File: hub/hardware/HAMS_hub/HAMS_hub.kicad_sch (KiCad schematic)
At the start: 29 parts, among them J1 Conn_01x14, J2 Conn_01x04, J3 Conn_01x04, J4 Conn_01x07, J5 Conn_01x02, J6 Conn_01x04, J7 Conn_01x04, J8 Conn_01x04, J9 Conn_01x04, Q1 NMOS, SW1 SW_Push, U1 TCA9406DC, U2 NCP5501, U3 NRF24L01_Breakout

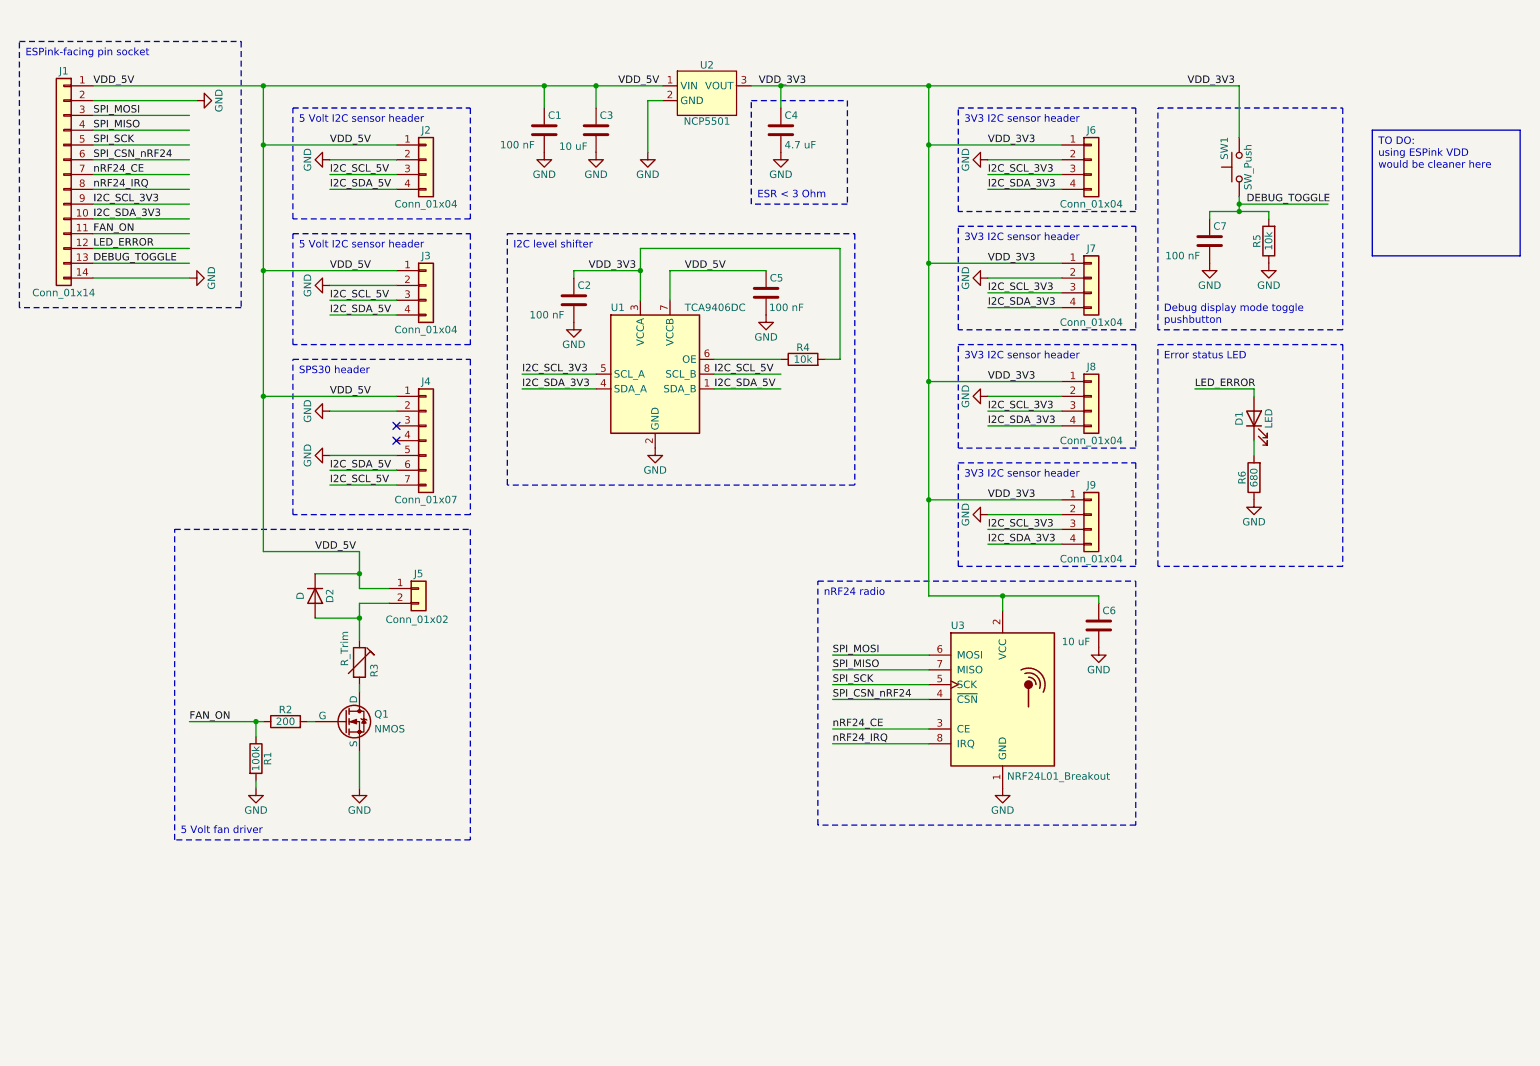
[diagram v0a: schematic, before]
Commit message: Improve HAMS hub HW: schematic and PCB
Improve schematic (add debug headers and mounting holes).
Add DRC-clean PCB design.
Update task list.
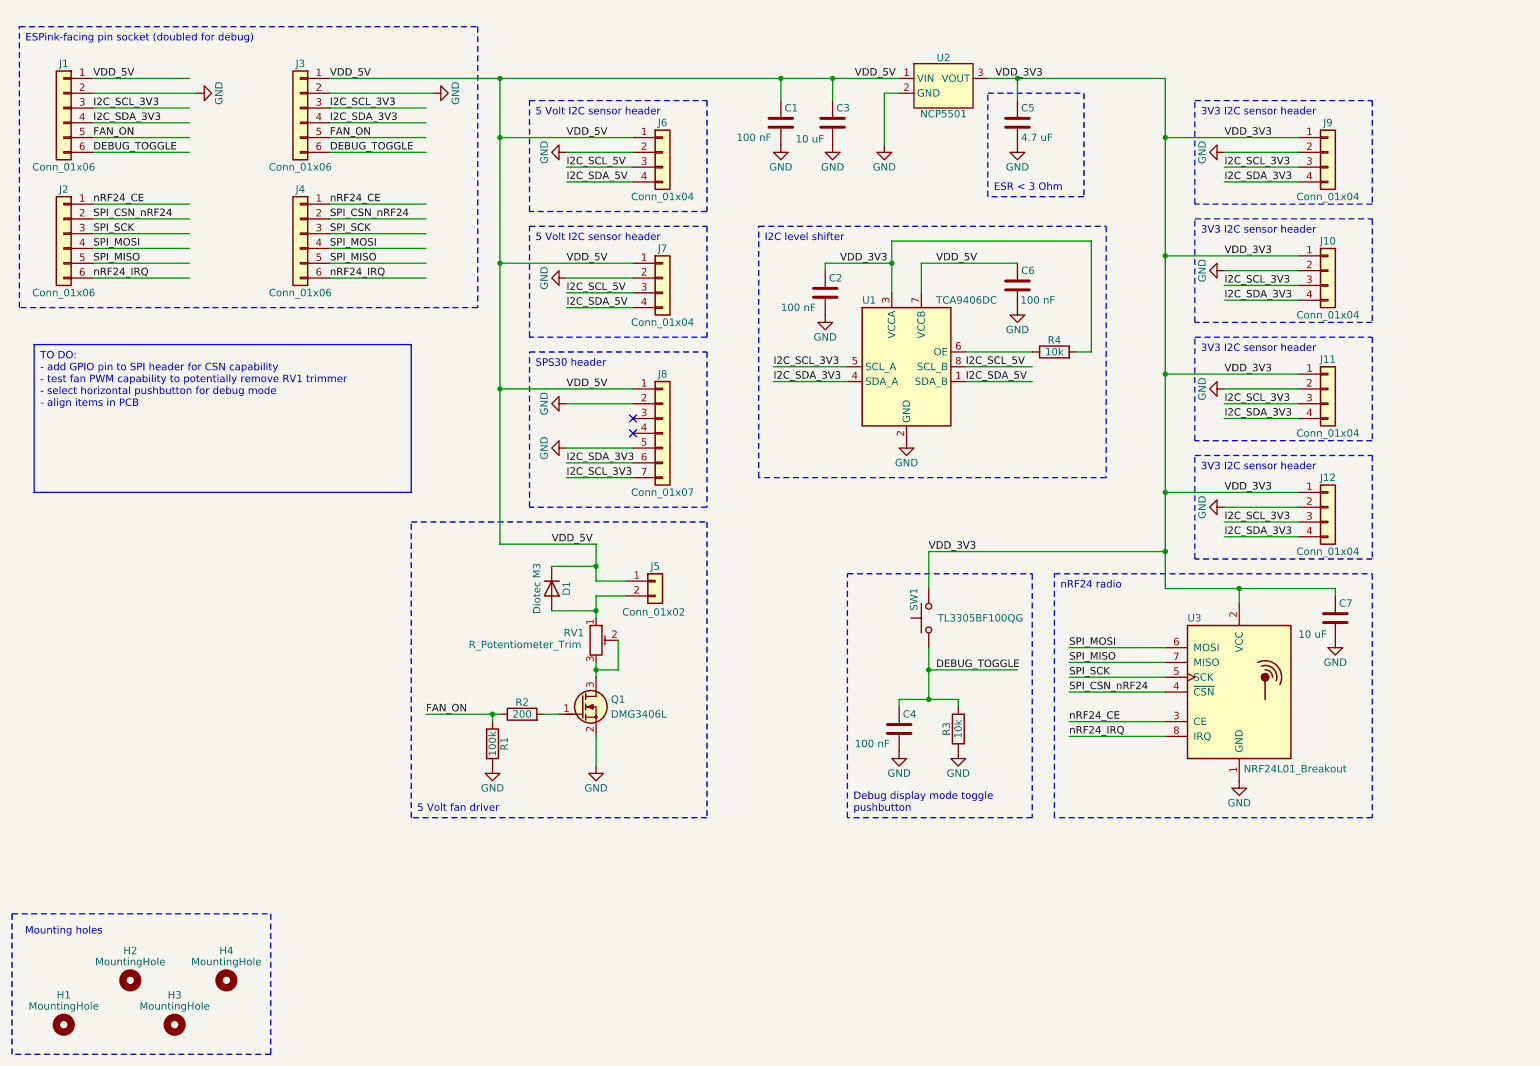
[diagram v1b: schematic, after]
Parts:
- removed D1: LED, symbol Device:LED
- removed J1: Conn_01x14, symbol Connector_Generic:Conn_01x14
- removed Q1: NMOS, symbol Simulation_SPICE:NMOS
- removed R3: R_Trim, symbol Device:R_Trim
- removed R6: 680, symbol Device:R
- added H1, H2, H3, H4: MountingHole, MountingHole:MountingHole_2.5mm, symbol Mechanical:MountingHole
- added J1, J2, J3, J4: Conn_01x06, Connector_PinSocket_2.54mm:PinSocket_1x06_P2.54mm_Vertical, symbol Connector_Generic:Conn_01x06
- added Q1: DMG3406L, PCM_Package_TO_SOT_SMD_AKL:SOT-23, symbol PCM_Transistor_MOSFET_AKL:DMG3406L
- added RV1: R_Potentiometer_Trim, PCM_Potentiometer_SMD_AKL:Potentiometer_Bourns_3269W_Vertical, symbol Device:R_Potentiometer_Trim
- C1, C2, C3: footprint (none) -> Capacitor_SMD:C_0805_2012Metric_Pad1.18x1.45mm_HandSolder
- C4: renamed from C7; footprint (none) -> Capacitor_SMD:C_0805_2012Metric_Pad1.18x1.45mm_HandSolder
- C5: renamed from C4; footprint (none) -> Capacitor_SMD:C_0805_2012Metric_Pad1.18x1.45mm_HandSolder
- C6: renamed from C5; footprint (none) -> Capacitor_SMD:C_0805_2012Metric_Pad1.18x1.45mm_HandSolder
- C7: renamed from C6; footprint (none) -> Capacitor_SMD:C_0805_2012Metric_Pad1.18x1.45mm_HandSolder
- D1: renamed from D2; value D -> Diotec M3; footprint (none) -> Diode_SMD:D_SMA_Handsoldering
- J10: renamed from J7; footprint (none) -> Connector_PinSocket_2.54mm:PinSocket_1x04_P2.54mm_Vertical
- J11: renamed from J8; footprint (none) -> Connector_PinSocket_2.54mm:PinSocket_1x04_P2.54mm_Vertical
- J12: renamed from J9; footprint (none) -> Connector_PinSocket_2.54mm:PinSocket_1x04_P2.54mm_Vertical
- J5: footprint (none) -> Connector_PinHeader_2.54mm:PinHeader_1x02_P2.54mm_Vertical
- J6: renamed from J2; footprint (none) -> Connector_PinSocket_2.54mm:PinSocket_1x04_P2.54mm_Vertical
- J7: renamed from J3; footprint (none) -> Connector_PinSocket_2.54mm:PinSocket_1x04_P2.54mm_Vertical
- J8: renamed from J4; footprint (none) -> Connector_PinHeader_2.54mm:PinHeader_1x07_P2.54mm_Vertical
- J9: renamed from J6; footprint (none) -> Connector_PinSocket_2.54mm:PinSocket_1x04_P2.54mm_Vertical
- R1, R2, R4: footprint (none) -> Resistor_SMD:R_0805_2012Metric_Pad1.20x1.40mm_HandSolder
- R3: renamed from R5; footprint (none) -> Resistor_SMD:R_0805_2012Metric_Pad1.20x1.40mm_HandSolder
- SW1: value SW_Push -> TL3305BF100QG; footprint (none) -> Personal_Switches:E-Switch_TL3305BF100QG_Tactile_SPST
- U1: footprint (none) -> Package_SO:SSOP-8_2.95x2.8mm_P0.65mm
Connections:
- net DEBUG_TOGGLE: now also J1.6 (Pin_6), J3.6 (Pin_6)
- net FAN_ON: now also J1.5 (Pin_5), J3.5 (Pin_5)
- net GND: now also J1.2 (Pin_2), J3.2 (Pin_2), Q1.2 (S)
- net I2C_SCL_3V3: now also J8.7 (Pin_7), J1.3 (Pin_3), J3.3 (Pin_3)
- net I2C_SCL_5V: no longer J8.7 (Pin_7)
- net I2C_SDA_3V3: now also J8.6 (Pin_6), J1.4 (Pin_4), J3.4 (Pin_4)
- net I2C_SDA_5V: no longer J8.6 (Pin_6)
- net SPI_CSN_nRF24: now also J2.2 (Pin_2), J4.2 (Pin_2)
- net SPI_MISO: now also J2.5 (Pin_5), J4.5 (Pin_5)
- net SPI_MOSI: now also J2.4 (Pin_4), J4.4 (Pin_4)
- net SPI_SCK: now also J2.3 (Pin_3), J4.3 (Pin_3)
- net VDD_5V: now also J1.1 (Pin_1), J3.1 (Pin_1)
- net nRF24_CE: now also J2.1 (Pin_1), J4.1 (Pin_1)
- net nRF24_IRQ: now also J2.6 (Pin_6), J4.6 (Pin_6)
- net at D1.2 (A), J5.2 (Pin_2): now also RV1.1
- net at R2.2: now also Q1.1 (G)
- new net: Q1.3 (D), RV1.2, RV1.3
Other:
- note added: "Mounting holes"
- moved on the sheet: C1, C2, C3, C4, C5, C6, C7, D1, J10, J11, J12, J5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

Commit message: Improve HAMS hub & node HW: schematic and PCB
Finalize hub and node PCB layouts & schematics.
Update task list.
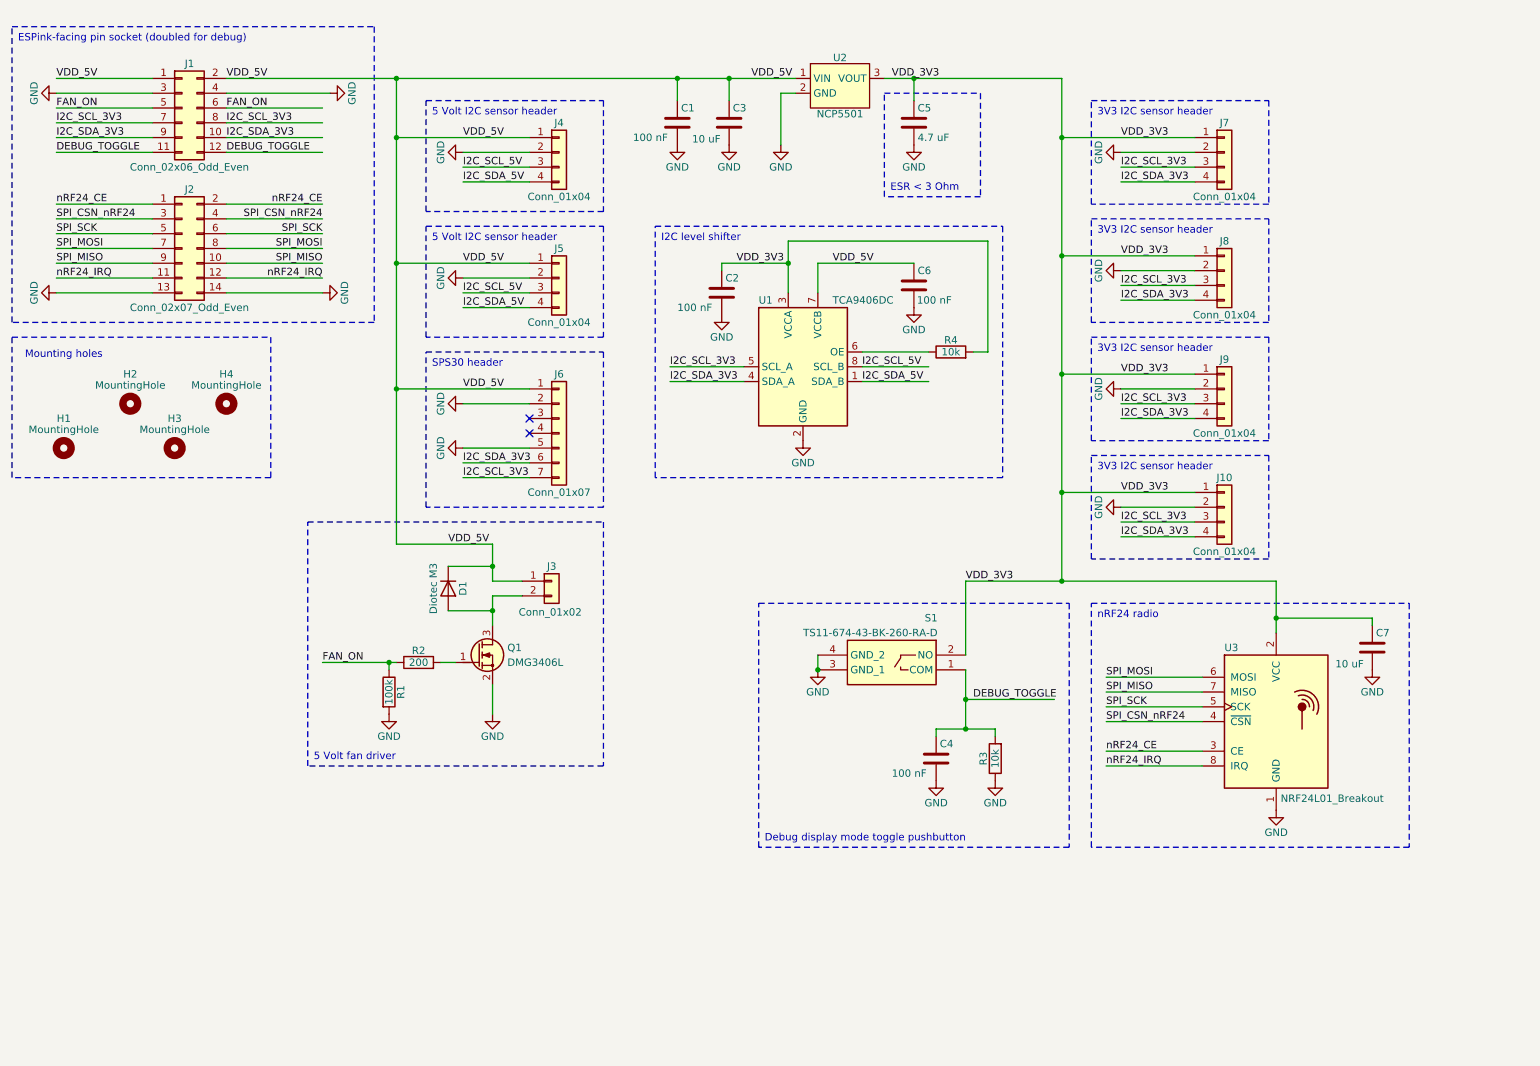
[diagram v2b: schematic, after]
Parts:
- removed J1, J2, J3, J4: Conn_01x06, Connector_PinSocket_2.54mm:PinSocket_1x06_P2.54mm_Vertical, symbol Connector_Generic:Conn_01x06
- removed RV1: R_Potentiometer_Trim, PCM_Potentiometer_SMD_AKL:Potentiometer_Bourns_3269W_Vertical, symbol Device:R_Potentiometer_Trim
- removed SW1: TL3305BF100QG, Personal_Switches:E-Switch_TL3305BF100QG_Tactile_SPST, symbol Switch:SW_Push
- added J1: Conn_02x06_Odd_Even, Connector_PinSocket_2.54mm:PinSocket_2x06_P2.54mm_Vertical, symbol Connector_Generic:Conn_02x06_Odd_Even
- added J2: Conn_02x07_Odd_Even, Connector_PinSocket_2.54mm:PinSocket_2x07_P2.54mm_Vertical, symbol Connector_Generic:Conn_02x07_Odd_Even
- added S1: TS11-674-43-BK-260-RA-D, Personal_SamacSys:TS1167443BK260RAD, symbol Personal_SamacSys:TS11-674-43-BK-260-RA-D
- renumbered J12 to J10, J5 to J3, J6 to J4, J7 to J5, J8 to J6, J9 to J7, J10 to J8, J11 to J9
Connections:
- net DEBUG_TOGGLE: now also J1.11 (Pin_11), J1.12 (Pin_12), S1.1 (COM)
- net FAN_ON: now also J1.5 (Pin_5), J1.6 (Pin_6)
- net GND: now also J1.3 (Pin_3), J1.4 (Pin_4), J2.13 (Pin_13), J2.14 (Pin_14), S1.3 (GND_1), S1.4 (GND_2)
- net I2C_SCL_3V3: now also J1.7 (Pin_7), J1.8 (Pin_8)
- net I2C_SDA_3V3: now also J1.10 (Pin_10), J1.9 (Pin_9)
- net SPI_CSN_nRF24: now also J2.3 (Pin_3), J2.4 (Pin_4)
- net SPI_MISO: now also J2.10 (Pin_10), J2.9 (Pin_9)
- net SPI_MOSI: now also J2.7 (Pin_7), J2.8 (Pin_8)
- net SPI_SCK: now also J2.5 (Pin_5), J2.6 (Pin_6)
- net VDD_3V3: now also S1.2 (NO)
- net VDD_5V: now also J1.1 (Pin_1), J1.2 (Pin_2)
- net nRF24_CE: now also J2.1 (Pin_1), J2.2 (Pin_2)
- net nRF24_IRQ: now also J2.11 (Pin_11), J2.12 (Pin_12)
- net at D1.2 (A), J3.2 (Pin_2): now also Q1.3 (D)
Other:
- moved on the sheet: C1, C2, C3, C4, C5, C6, C7, D1, H1, H2, H3, H4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

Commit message: Improve HAMS hub HW: reset button
Add reset button.
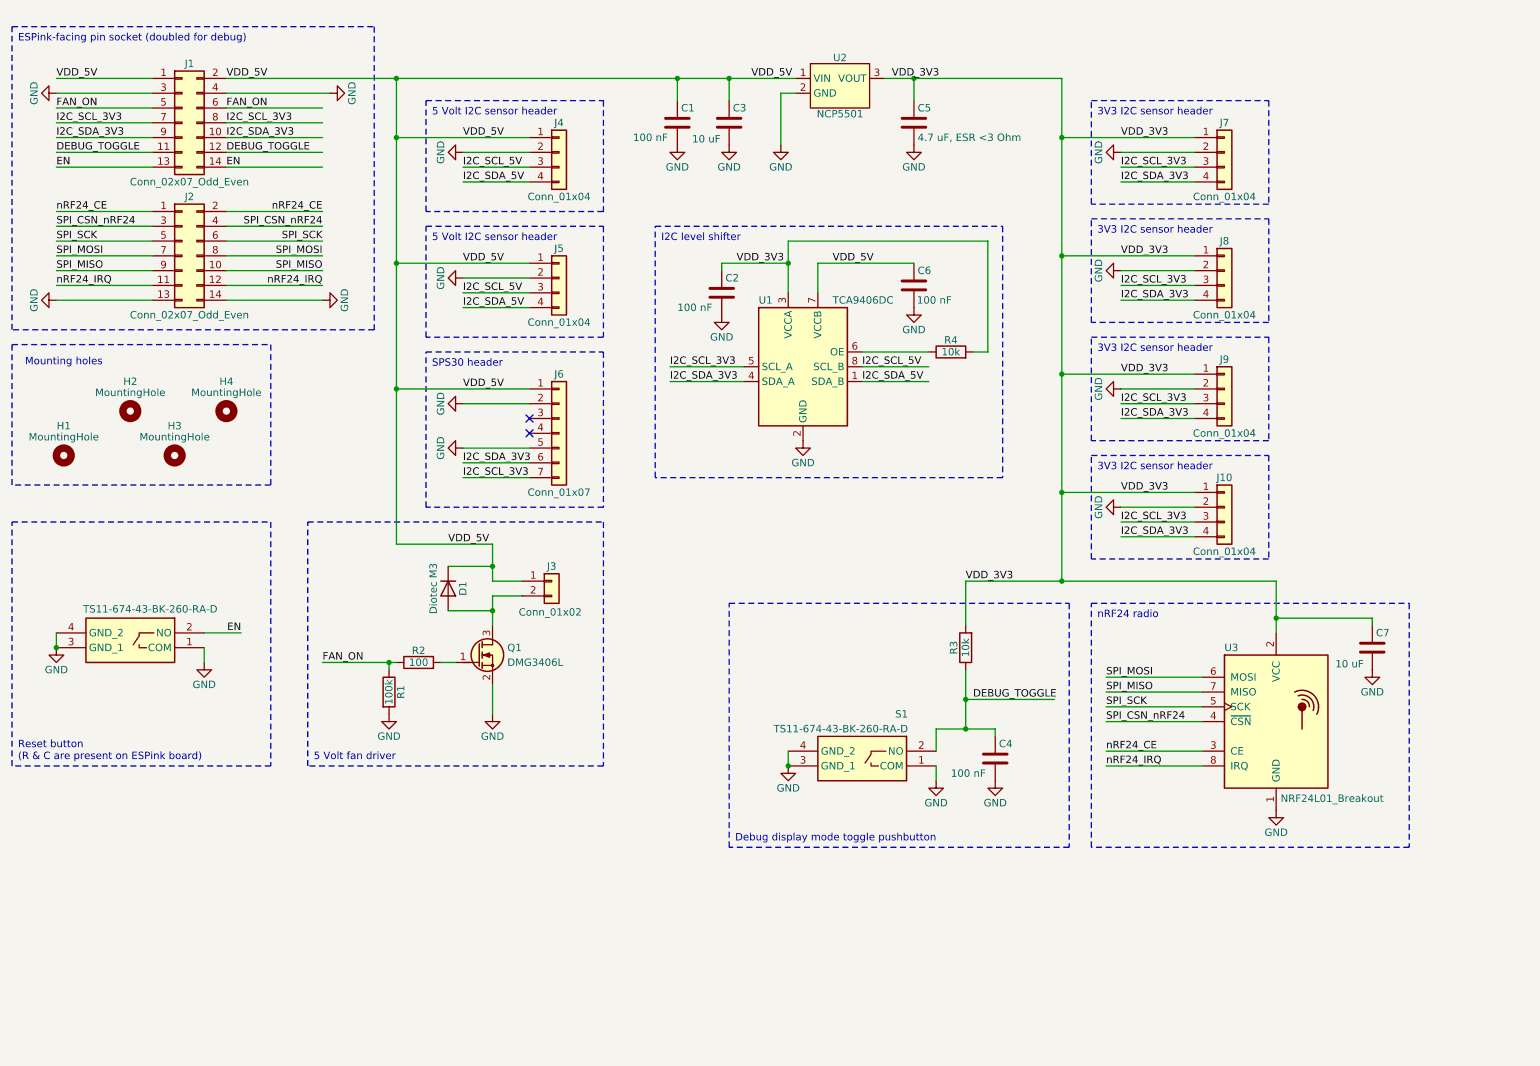
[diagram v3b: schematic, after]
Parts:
- removed J1: Conn_02x06_Odd_Even, Connector_PinSocket_2.54mm:PinSocket_2x06_P2.54mm_Vertical, symbol Connector_Generic:Conn_02x06_Odd_Even
- added J1: Conn_02x07_Odd_Even, Connector_PinSocket_2.54mm:PinSocket_2x07_P2.54mm_Vertical, symbol Connector_Generic:Conn_02x07_Odd_Even
- added S2: TS11-674-43-BK-260-RA-D, Personal_SamacSys:TS1167443BK260RAD, symbol Personal_SamacSys:TS11-674-43-BK-260-RA-D
- C5: value 4.7 uF -> 4.7 uF, ESR <3 Ohm
- H1, H2, H3, H4: footprint MountingHole:MountingHole_2.5mm -> MountingHole:MountingHole_2.2mm_M2_ISO7380
- R2: value 200 -> 100
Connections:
- net DEBUG_TOGGLE: now also R3.1, S1.2 (NO), J1.11 (Pin_11), J1.12 (Pin_12); no longer R3.2, S1.1 (COM)
- net FAN_ON: now also J1.5 (Pin_5), J1.6 (Pin_6)
- net GND: now also S1.1 (COM), J1.3 (Pin_3), J1.4 (Pin_4), S2.1 (COM), S2.3 (GND_1), S2.4 (GND_2); no longer R3.1
- net I2C_SCL_3V3: now also J1.7 (Pin_7), J1.8 (Pin_8)
- net I2C_SDA_3V3: now also J1.10 (Pin_10), J1.9 (Pin_9)
- net VDD_3V3: now also R3.2; no longer S1.2 (NO)
- net VDD_5V: now also J1.1 (Pin_1), J1.2 (Pin_2)
- new net EN: J1.13 (Pin_13), J1.14 (Pin_14), S2.2 (NO)
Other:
- moved on the sheet: C4, H1, H2, H3, H4, J2, R3, S1
